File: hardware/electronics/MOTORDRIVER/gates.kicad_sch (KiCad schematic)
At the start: 39 parts, among them IC14 LM5109BSDX_NOPB, IC15 LM5109BSDX_NOPB, IC16 LM5109BSDX_NOPB, IC17 LM5109BSDX_NOPB, IC18 INA2181A2IDGSR, Q22 30V 71A, Q23 30V 71A, Q24 30V 71A, Q25 30V 71A, Q26 30V 71A, Q27 30V 71A, Q28 30V 71A

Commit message: had to redo some work :<
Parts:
- renumbered C148 to C149, C149 to C150, C150 to C151, C151 to C152, C152 to C153, C153 to C154, C154 to C155, C155 to C156, C156 to C157

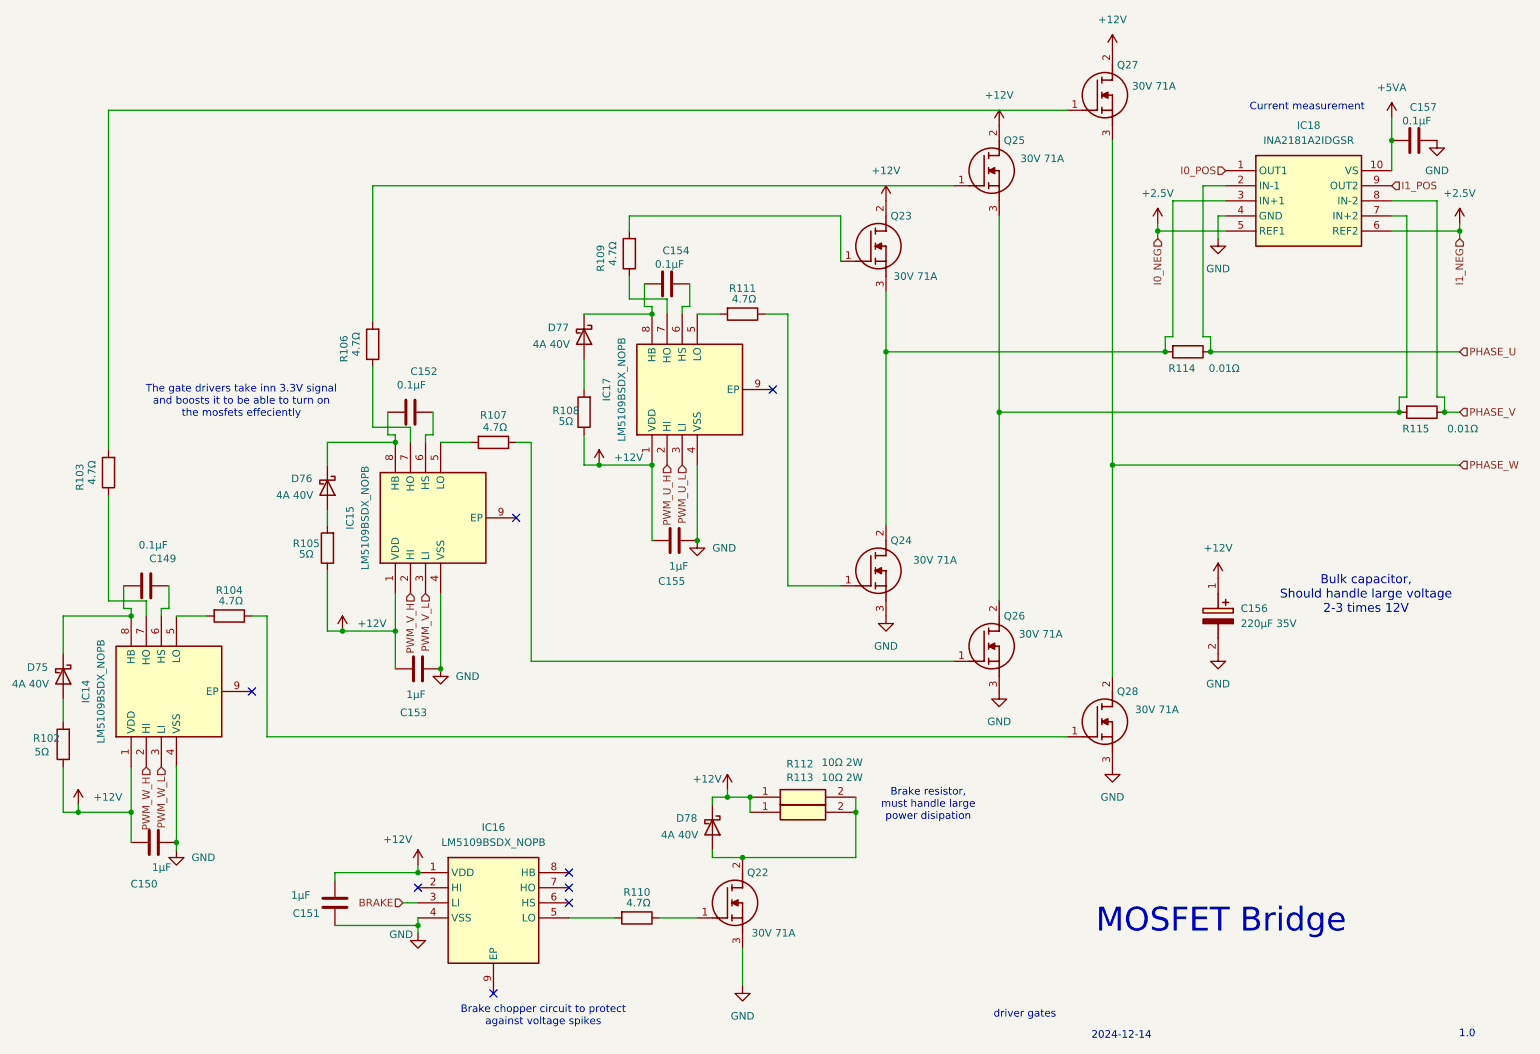
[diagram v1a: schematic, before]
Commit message: worked on pcb and added led to programmer and jumpers to swd line
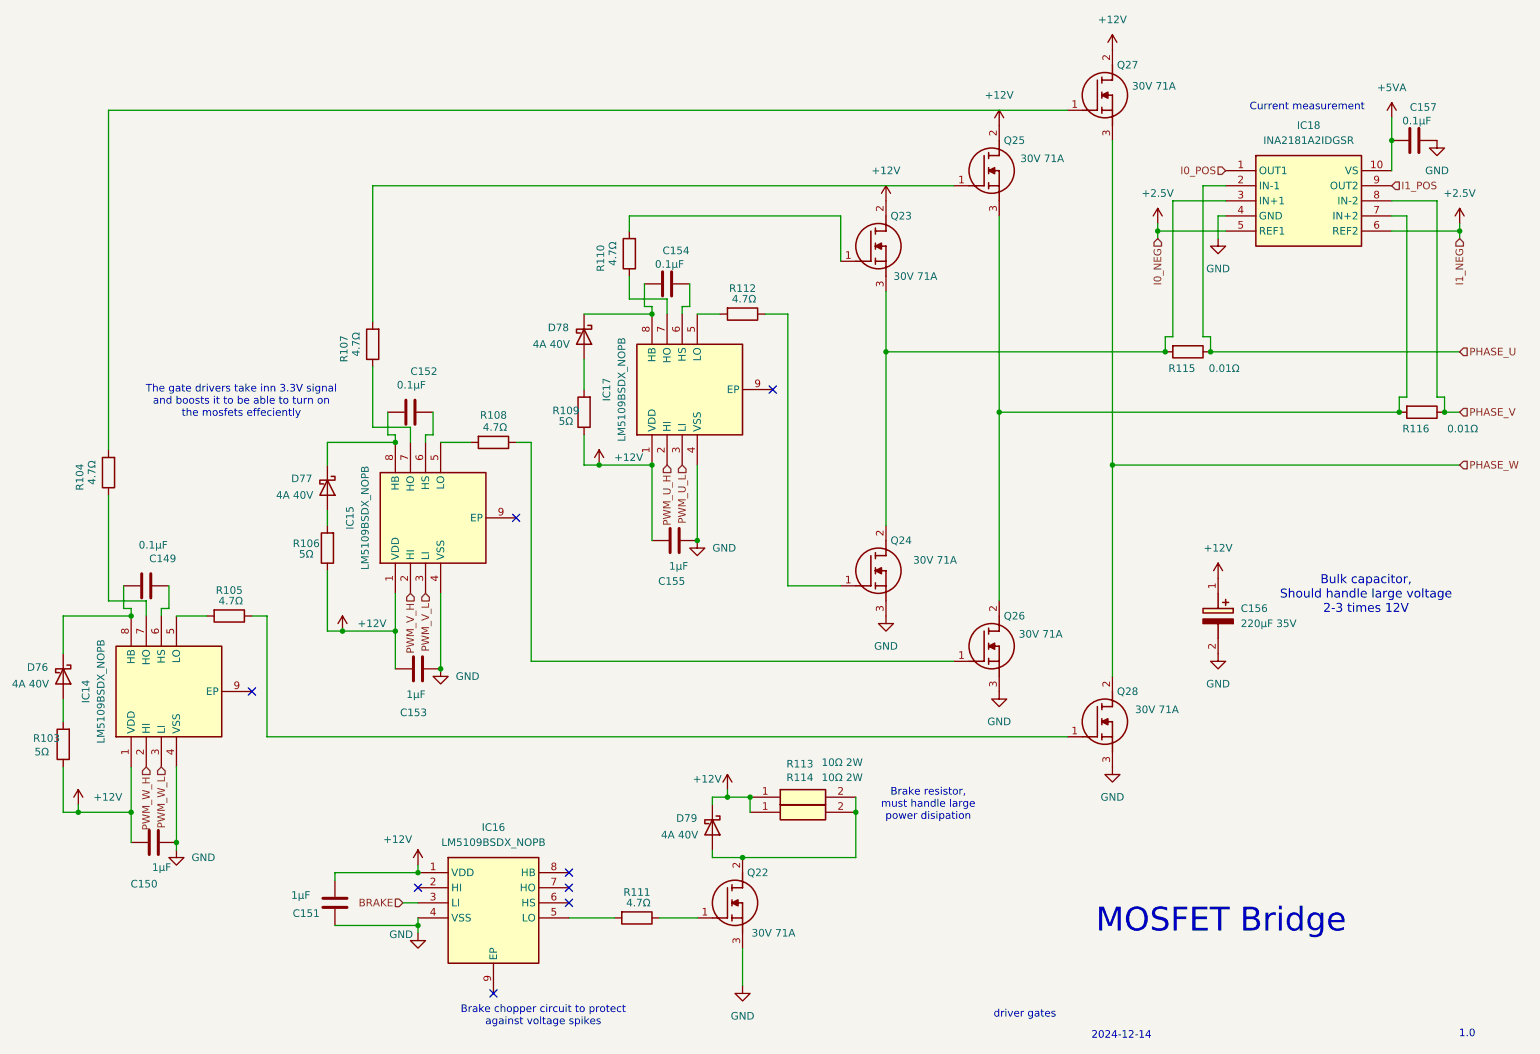
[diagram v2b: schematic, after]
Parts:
- renumbered D75 to D76, D76 to D77, D77 to D78, D78 to D79, R102 to R103, R103 to R104, R104 to R105, R105 to R106, R106 to R107, R107 to R108, R108 to R109, R109 to R110, R110 to R111, R111 to R112, R112 to R113, R113 to R114, R114 to R115, R115 to R116
